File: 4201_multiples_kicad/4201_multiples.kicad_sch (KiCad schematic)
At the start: 41 parts, among them J1 Conn_02x05_Odd_Even, J2 PJ398SM, J3 PJ398SM, J4 PJ398SM, J5 PJ398SM, J6 PJ398SM, J7 PJ398SM, J8 PJ398SM, J9 PJ398SM, U1 TL074, U2 TL074

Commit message: Continue work on PCB layouts
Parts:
- removed C1, C2: 47uF, Capacitor_SMD:CP_Elec_5x5.3, symbol Device:C_Polarized
- removed C3, C4, C5, C6: 100nF, Capacitor_SMD:C_1206_3216Metric_Pad1.33x1.80mm_HandSolder, symbol Device:C
- removed D1, D2, D3, D4, D5, D6, D7, D8: 1N4148, Diode_SMD:D_1206_3216Metric_Pad1.42x1.75mm_HandSolder, symbol Diode:1N4007
- removed D10, D12: 1.8mm_red, LED_THT:LED_D1.8mm_W3.3mm_H2.4mm, symbol Device:LED
- removed D11, D9: 1.8mm_green, LED_THT:LED_D1.8mm_W3.3mm_H2.4mm, symbol Device:LED
- removed J1: Conn_02x05_Odd_Even, Connector_IDC:IDC-Header_2x05_P2.54mm_Vertical, symbol Connector_Generic:Conn_02x05_Odd_Even
- removed J2, J3, J4, J5, J6, J7, J8, J9: PJ398SM, 4ms_Jack:EighthInch_PJ398SM, symbol 4ms_Jack:3.5mm_Mono_Switched_sm
- removed R1, R2: 220k, Resistor_SMD:R_1206_3216Metric_Pad1.30x1.75mm_HandSolder, symbol Device:R
- removed R10, R12: 4k7, Resistor_SMD:R_1206_3216Metric_Pad1.30x1.75mm_HandSolder, symbol Device:R
- removed R11, R9: 39k, Resistor_SMD:R_1206_3216Metric_Pad1.30x1.75mm_HandSolder, symbol Device:R
- removed R3, R4, R5, R6, R7, R8: 100R, Resistor_SMD:R_1206_3216Metric_Pad1.30x1.75mm_HandSolder, symbol Device:R
- removed U1, U2: TL074, Package_SO:SOIC-14_3.9x8.7mm_P1.27mm, symbol Amplifier_Operational:TL074
- added J10: Conn_01x03_Female, symbol Connector:Conn_01x03_Female
- added J11: Conn_01x04_Female, Connector_PinSocket_2.54mm:PinSocket_1x04_P2.54mm_Vertical, symbol Connector:Conn_01x04_Female
- added J12: Conn_01x03_Female, Connector_PinSocket_2.54mm:PinSocket_1x03_P2.54mm_Vertical, symbol Connector:Conn_01x03_Female
- added J13: Conn_01x05_Male, symbol Connector:Conn_01x05_Male
- added J14: Conn_01x03_Male, symbol Connector:Conn_01x03_Male
- added J15: Conn_01x04_Male, Connector_PinHeader_2.54mm:PinHeader_1x04_P2.54mm_Vertical, symbol Connector:Conn_01x04_Male
- added J16: Conn_01x03_Male, Connector_PinHeader_2.54mm:PinHeader_1x03_P2.54mm_Vertical, symbol Connector:Conn_01x03_Male
- added J9: Conn_01x05_Female, symbol Connector:Conn_01x05_Female
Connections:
- new net interface/0V: J9.5 (Pin_5)
- new net interface/IN_1: J9.1 (Pin_1)
- new net interface/IN_2: J11.1 (Pin_1)
- new net interface/LED_1N_K: J10.2 (Pin_2)
- new net interface/LED_1P_A: J10.1 (Pin_1)
- new net interface/LED_1_PK_NA: J10.3 (Pin_3)
- new net interface/LED_2N_K: J12.2 (Pin_2)
- new net interface/LED_2P_A: J12.1 (Pin_1)
- new net interface/LED_2_PK_NA: J12.3 (Pin_3)
- new net interface/OUT_1_1: J9.2 (Pin_2)
- new net interface/OUT_1_2: J9.3 (Pin_3)
- new net interface/OUT_1_3: J9.4 (Pin_4)
- new net interface/OUT_2_1: J11.2 (Pin_2)
- new net interface/OUT_2_2: J11.3 (Pin_3)
- new net interface/OUT_2_3: J11.4 (Pin_4)
- new net main_board/0V: J13.5 (Pin_5)
- new net main_board/IN_1: J13.1 (Pin_1)
- new net main_board/IN_2: J15.1 (Pin_1)
- new net main_board/LED_1N_K: J14.2 (Pin_2)
- new net main_board/LED_1P_A: J14.1 (Pin_1)
- new net main_board/LED_1_PK_NA: J14.3 (Pin_3)
- new net main_board/LED_2N_K: J16.2 (Pin_2)
- new net main_board/LED_2P_A: J16.1 (Pin_1)
- new net main_board/LED_2_PK_NA: J16.3 (Pin_3)
- new net main_board/OUT_1_1: J13.2 (Pin_2)
- new net main_board/OUT_1_2: J13.3 (Pin_3)
- new net main_board/OUT_1_3: J13.4 (Pin_4)
- new net main_board/OUT_2_1: J15.2 (Pin_2)
- new net main_board/OUT_2_2: J15.3 (Pin_3)
- new net main_board/OUT_2_3: J15.4 (Pin_4)
- no-connect marks 8 -> 0
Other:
- added sheet interface (interface.kicad_sch)
- added sheet main_board (main_board.kicad_sch)

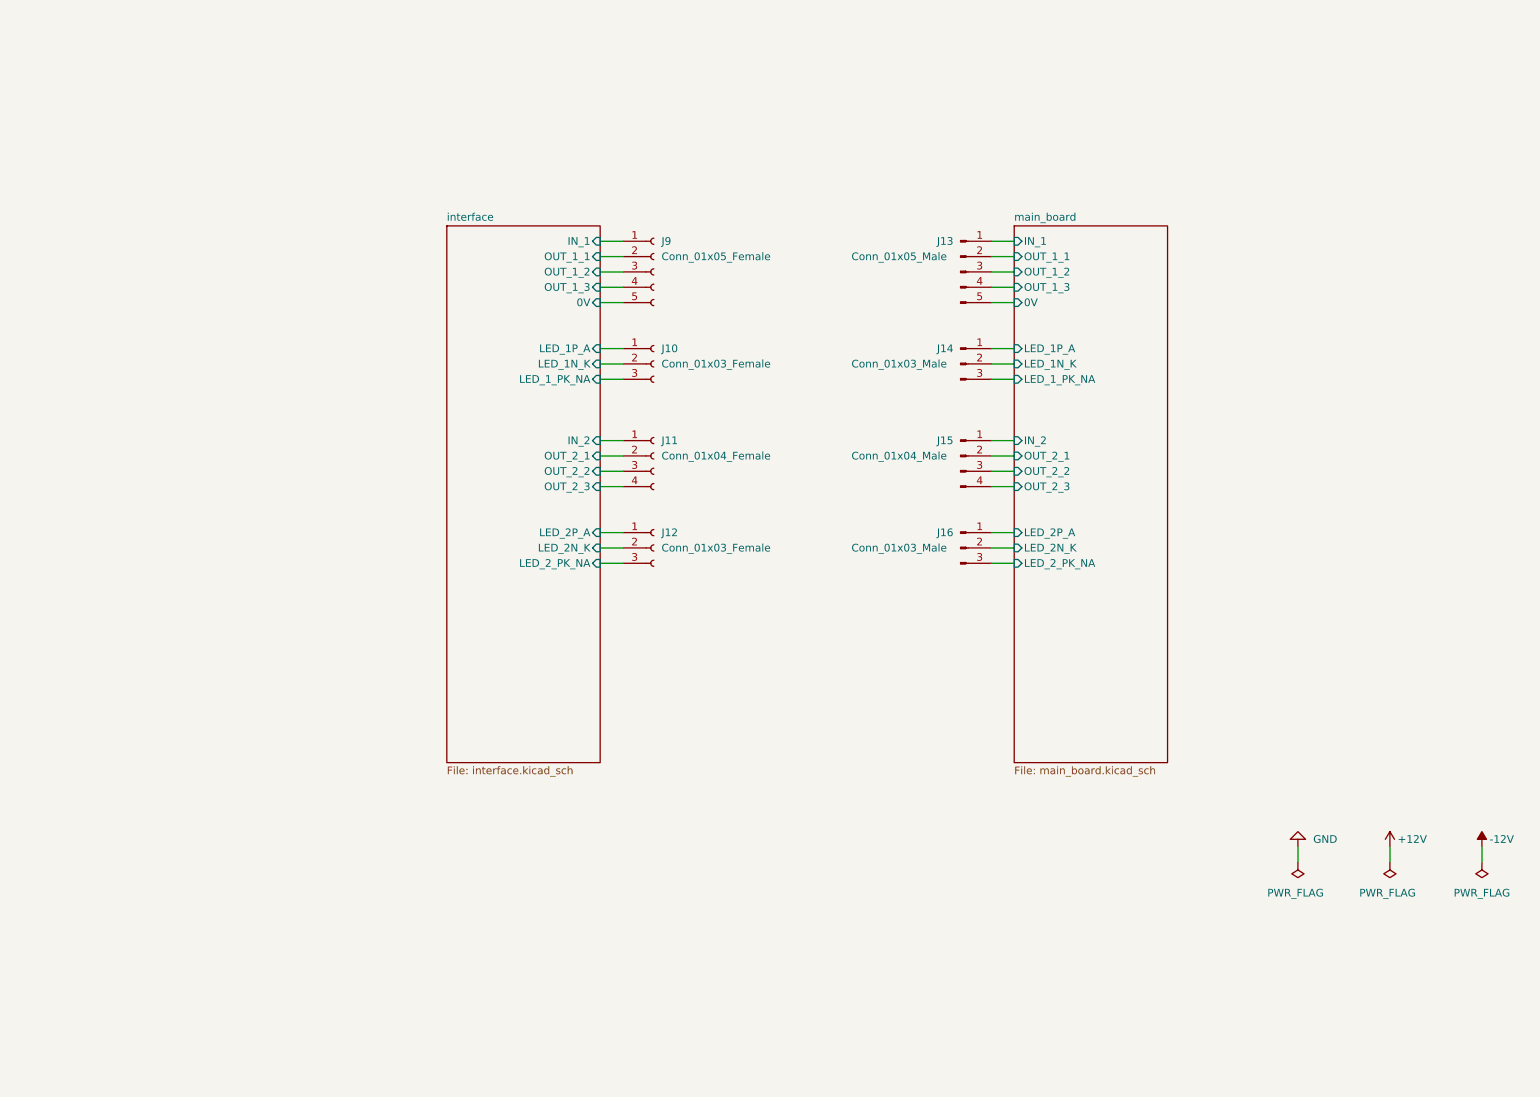
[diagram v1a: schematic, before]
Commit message: Finish layout first draft
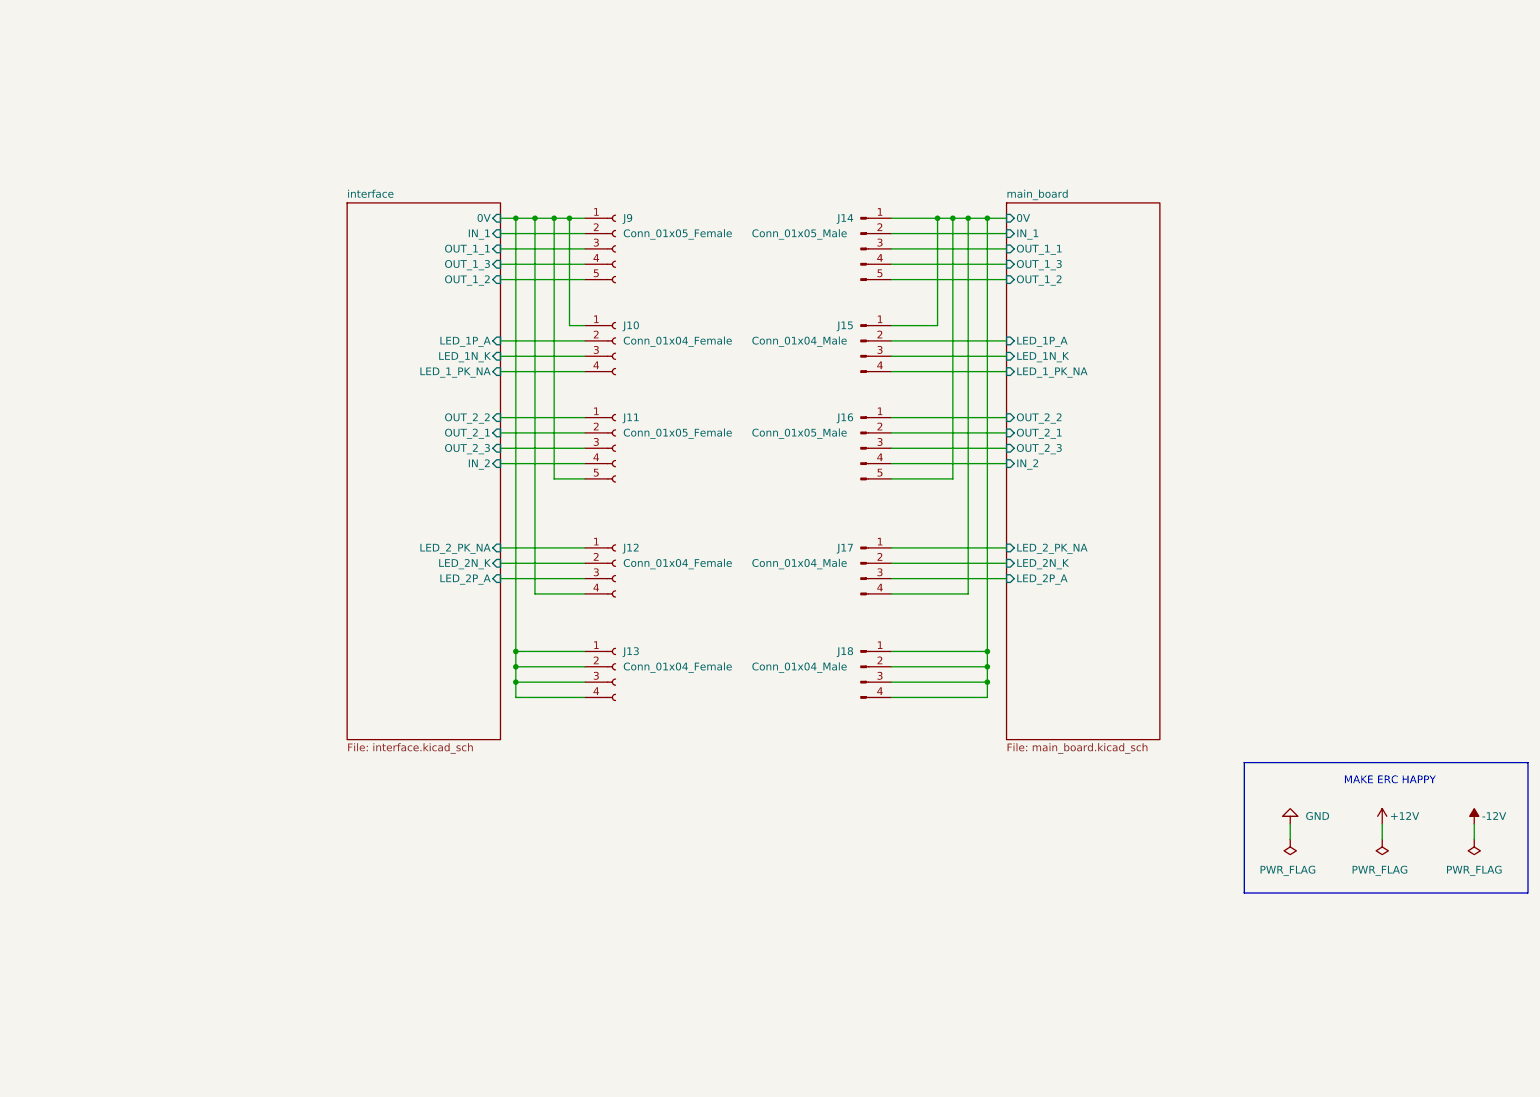
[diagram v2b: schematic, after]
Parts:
- removed J10: Conn_01x03_Female, symbol Connector:Conn_01x03_Female
- removed J11: Conn_01x04_Female, Connector_PinSocket_2.54mm:PinSocket_1x04_P2.54mm_Vertical, symbol Connector:Conn_01x04_Female
- removed J12: Conn_01x03_Female, Connector_PinSocket_2.54mm:PinSocket_1x03_P2.54mm_Vertical, symbol Connector:Conn_01x03_Female
- removed J14: Conn_01x03_Male, symbol Connector:Conn_01x03_Male
- removed J16: Conn_01x03_Male, Connector_PinHeader_2.54mm:PinHeader_1x03_P2.54mm_Vertical, symbol Connector:Conn_01x03_Male
- added J10, J12, J13: Conn_01x04_Female, Connector_PinSocket_2.54mm:PinSocket_1x04_P2.54mm_Vertical, symbol Connector:Conn_01x04_Female
- added J11: Conn_01x05_Female, Connector_PinSocket_2.54mm:PinSocket_1x05_P2.54mm_Vertical, symbol Connector:Conn_01x05_Female
- added J16: Conn_01x05_Male, Connector_PinHeader_2.54mm:PinHeader_1x05_P2.54mm_Vertical, symbol Connector:Conn_01x05_Male
- added J17, J18: Conn_01x04_Male, Connector_PinHeader_2.54mm:PinHeader_1x04_P2.54mm_Vertical, symbol Connector:Conn_01x04_Male
- J14: renamed from J13; footprint (none) -> Connector_PinHeader_2.54mm:PinHeader_1x05_P2.54mm_Vertical
- J9: footprint (none) -> Connector_PinSocket_2.54mm:PinSocket_1x05_P2.54mm_Vertical
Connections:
- net interface/0V: now also J9.1 (Pin_1), J10.1 (Pin_1), J11.5 (Pin_5), J12.4 (Pin_4), J13.1 (Pin_1), J13.2 (Pin_2), J13.3 (Pin_3), J13.4 (Pin_4); no longer J9.5 (Pin_5)
- net interface/IN_1: now also J9.2 (Pin_2); no longer J9.1 (Pin_1)
- net interface/IN_2: now also J11.4 (Pin_4)
- net interface/LED_1N_K: now also J10.3 (Pin_3)
- net interface/LED_1P_A: now also J10.2 (Pin_2)
- net interface/LED_1_PK_NA: now also J10.4 (Pin_4)
- net interface/LED_2N_K: now also J12.2 (Pin_2)
- net interface/LED_2P_A: now also J12.3 (Pin_3)
- net interface/LED_2_PK_NA: now also J12.1 (Pin_1)
- net interface/OUT_1_1: now also J9.3 (Pin_3); no longer J9.2 (Pin_2)
- net interface/OUT_1_2: now also J9.5 (Pin_5); no longer J9.3 (Pin_3)
- net interface/OUT_2_1: now also J11.2 (Pin_2)
- net interface/OUT_2_2: now also J11.1 (Pin_1)
- net interface/OUT_2_3: now also J11.3 (Pin_3)
- net main_board/0V: now also J14.1 (Pin_1), J15.1 (Pin_1), J16.5 (Pin_5), J17.4 (Pin_4), J18.1 (Pin_1), J18.2 (Pin_2), J18.3 (Pin_3), J18.4 (Pin_4); no longer J14.5 (Pin_5)
- net main_board/IN_1: now also J14.2 (Pin_2); no longer J14.1 (Pin_1)
- net main_board/IN_2: now also J16.4 (Pin_4); no longer J15.1 (Pin_1)
- net main_board/LED_1N_K: now also J15.3 (Pin_3)
- net main_board/LED_1P_A: now also J15.2 (Pin_2)
- net main_board/LED_1_PK_NA: now also J15.4 (Pin_4)
- net main_board/LED_2N_K: now also J17.2 (Pin_2)
- net main_board/LED_2P_A: now also J17.3 (Pin_3)
- net main_board/LED_2_PK_NA: now also J17.1 (Pin_1)
- net main_board/OUT_1_1: now also J14.3 (Pin_3); no longer J14.2 (Pin_2)
- net main_board/OUT_1_2: now also J14.5 (Pin_5); no longer J14.3 (Pin_3)
- net main_board/OUT_2_1: now also J16.2 (Pin_2); no longer J15.2 (Pin_2)
- net main_board/OUT_2_2: now also J16.1 (Pin_1); no longer J15.3 (Pin_3)
- net main_board/OUT_2_3: now also J16.3 (Pin_3); no longer J15.4 (Pin_4)
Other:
- note added: "MAKE ERC HAPPY"
- moved on the sheet: J14, J9

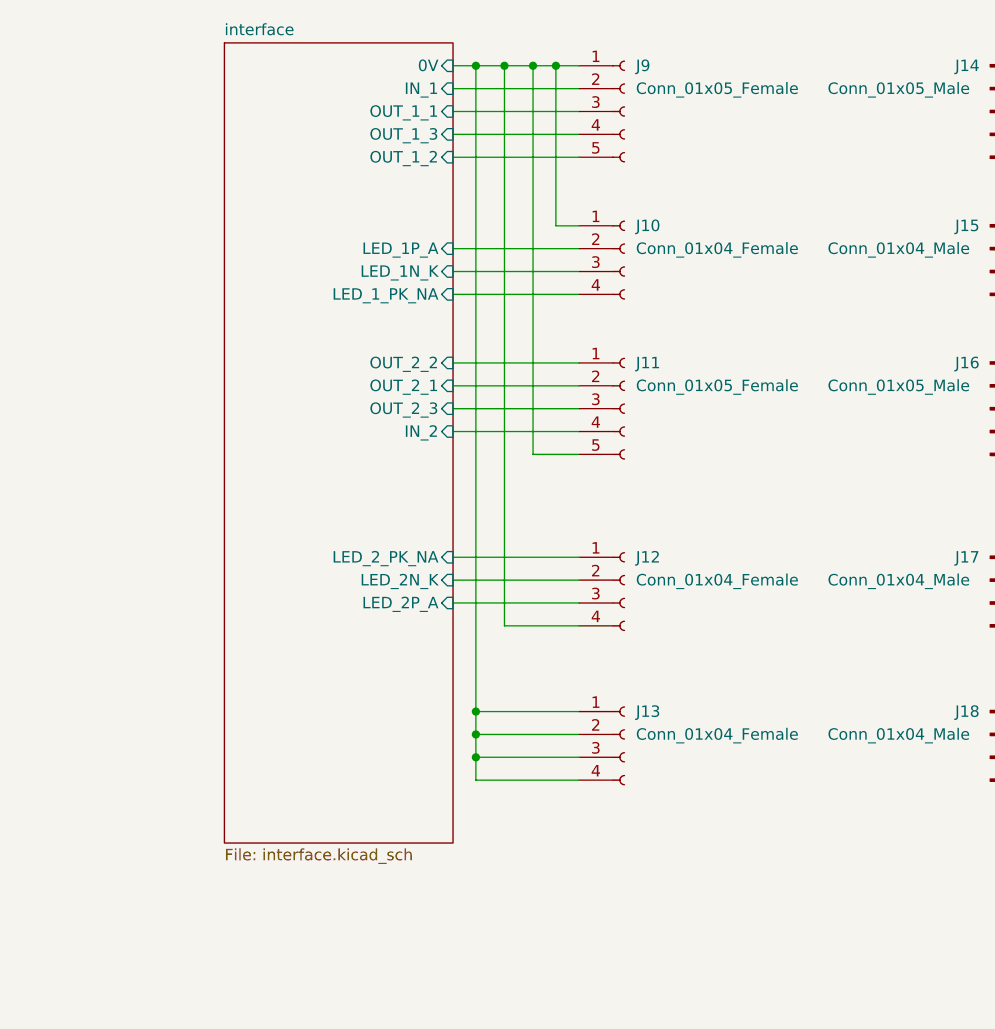
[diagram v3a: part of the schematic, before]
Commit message: Add stitching vias and clean up files
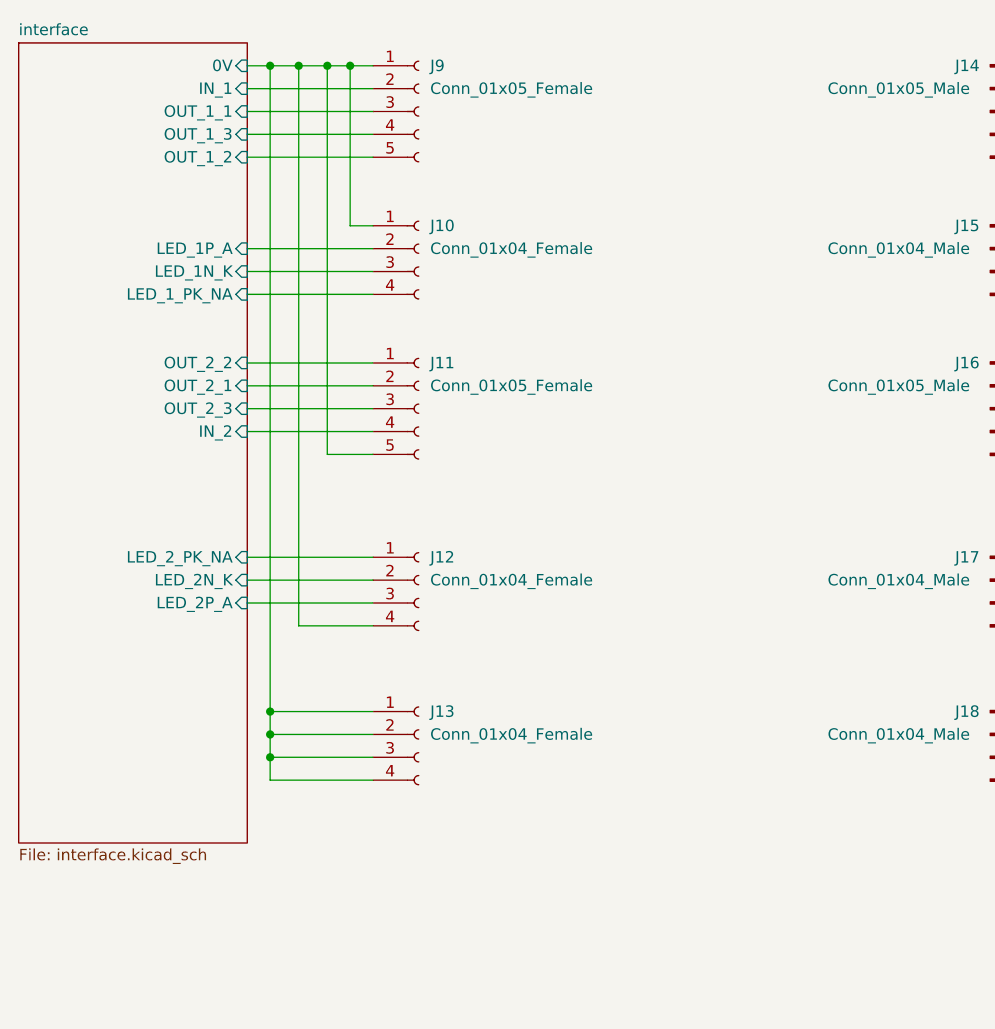
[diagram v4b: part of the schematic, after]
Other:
- moved on the sheet: J10, J11, J12, J13, J9
